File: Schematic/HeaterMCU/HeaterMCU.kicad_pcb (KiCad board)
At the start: 2 copper layers, 100 x 35 mm, 60 parts, among them J301 To PSU Board, J302 Heater Control, J303 High voltage warning, J304 Firmware, SW301 RESET, U301 Display_IPS_1.3_SPI, U302 ATMEGA328P-AU, U303 TLP185, U304 INA219AIDCNR, U305 TLP185, U306 TPS54302, Y301 8MHz

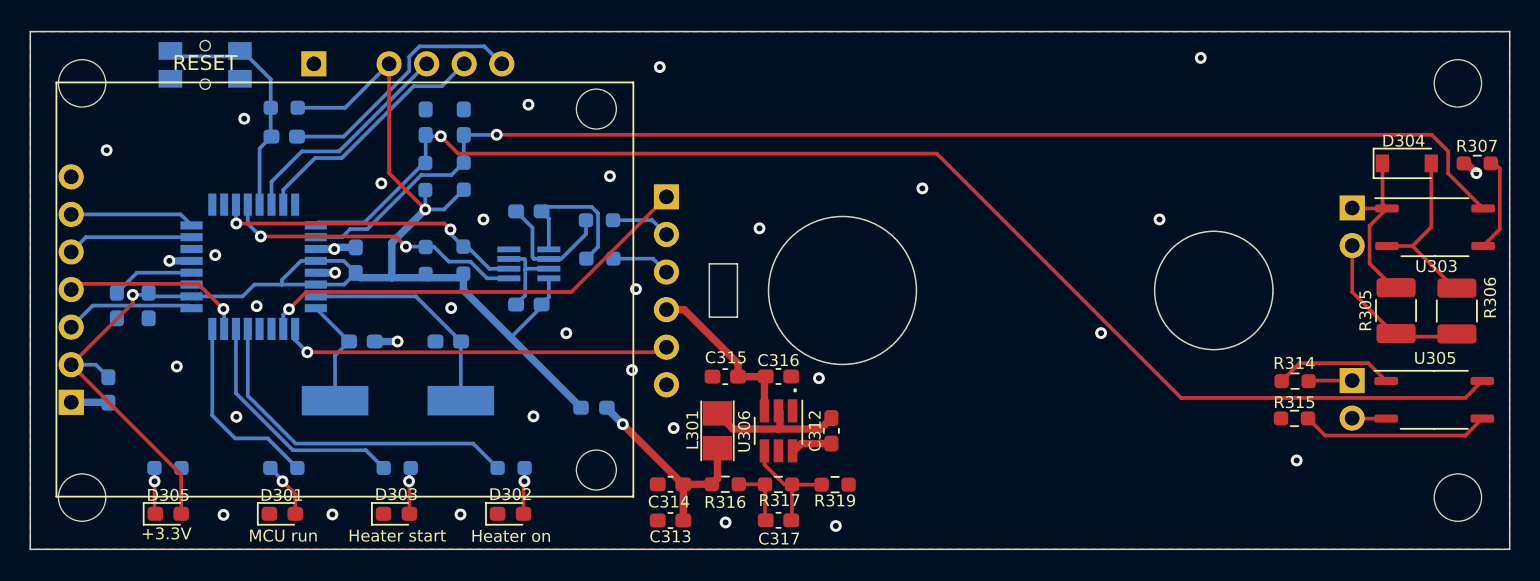
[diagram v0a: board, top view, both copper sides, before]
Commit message: New PSU based on XL4005
Added current limiter
Added interface to uTracer PIC
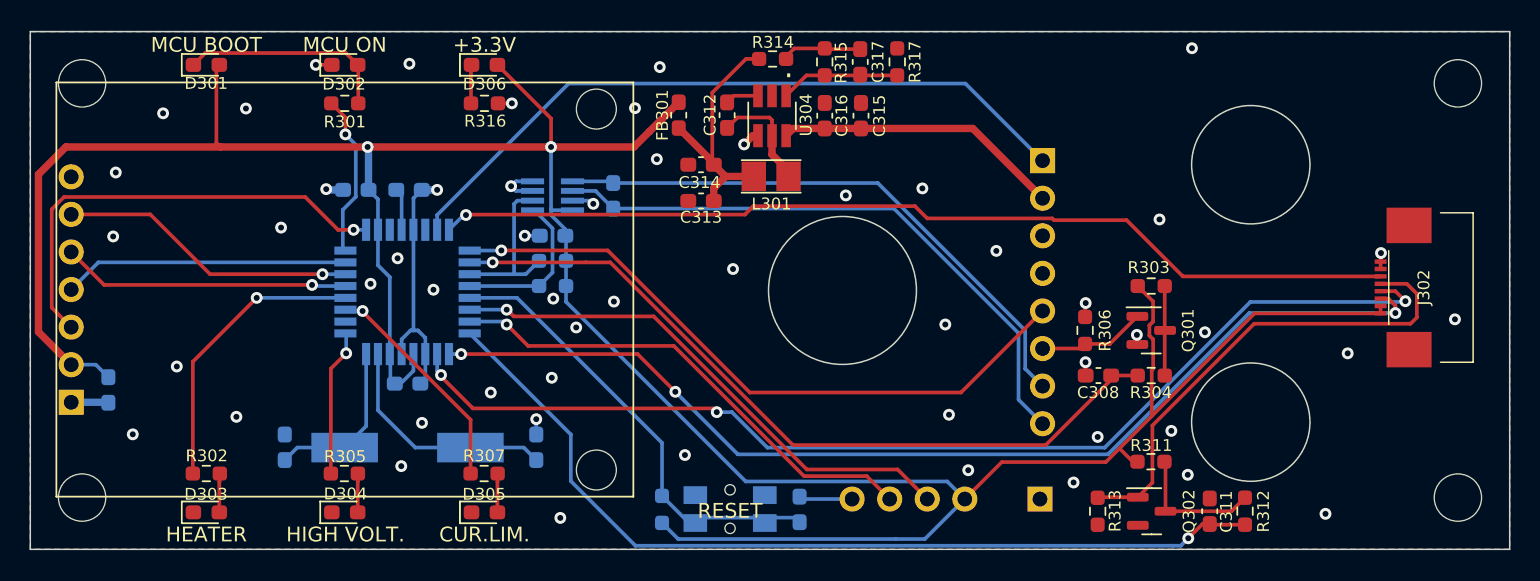
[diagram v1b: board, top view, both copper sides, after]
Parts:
- removed the C303 at (63.0, 63.5)
- removed the D304 at (148.0, 53.9)
- removed the J303 at (144.3, 68.6)
- removed the R305 at (147.3, 63.9)
- removed the R314 at (140.5, 68.6)
- removed the R315 at (140.5, 71.2)
- removed the U303 at (150.0, 58.2)
- removed U305: TLP185, Package_SO:SOIC-4_4.55x3.7mm_P2.54mm
- added C305: 100nF, Capacitor_SMD:C_0603_1608Metric_Pad1.08x0.95mm_HandSolder, B.Cu at (77.0, 55.7)
- added D301: "MCU_BOOT", LED_SMD:LED_0603_1608Metric_Pad1.05x0.95mm_HandSolder, F.Cu at (66.9, 47.2)
- added D305: "Current limit", LED_SMD:LED_0603_1608Metric_Pad1.05x0.95mm_HandSolder, F.Cu at (85.7, 77.5)
- added Q301: BSS138, Package_TO_SOT_SMD:SOT-23, F.Cu at (130.8, 65.2)
- added Q302: BSS138, Package_TO_SOT_SMD:SOT-23, F.Cu at (130.8, 77.4)
- added R303: 1MΩ, Resistor_SMD:R_0603_1608Metric_Pad0.98x0.95mm_HandSolder, F.Cu at (130.8, 62.2)
- C308, C311: value 220nF -> 1µF; moved to F.Cu
- D303: renamed from D302; value "Heater_ON" -> HEATER
- D304: renamed from D303; value "Heater_Start" -> "High Voltage"
- D306: renamed from D305; value "+5V" -> "+3.3V"
- FB301: moved to F.Cu
- J301: footprint Connector_PinSocket_2.54mm:PinSocket_1x06_P2.54mm_Vertical -> Connector_PinHeader_2.54mm:PinHeader_1x08_P2.54mm_Vertical
- J302: value Heater Control -> To µTracer; footprint Connector_PinSocket_2.54mm:PinSocket_1x02_P2.54mm_Horizontal -> myDevices:0527450897; moved to F.Cu
- R301, R302: value 560Ω -> 330Ω; moved to F.Cu
- R304, R312: value 1MΩ -> 220Ω; moved to F.Cu
- R305: renamed from R303; value 560Ω -> 330Ω; moved to F.Cu
- R306: value 3.9kΩ 1/2W -> 100kΩ; footprint Resistor_SMD:R_1210_3225Metric_Pad1.30x2.65mm_HandSolder -> Resistor_SMD:R_0603_1608Metric_Pad0.98x0.95mm_HandSolder
- R307: value 220Ω -> 330Ω
- R311: value 10Ω -> 1MΩ; moved to F.Cu
- R313: value 10Ω -> 100kΩ; moved to F.Cu
- R316: renamed from R318; moved to F.Cu
- moved R307 70.3 mm to (85.7, 74.9), turned to 180 degrees
- moved R312 59.8 mm to (137.1, 77.4)
- moved C311 59.2 mm to (134.7, 77.4)
- moved J303 57.2 mm to (123.2, 76.6), turned to 90 degrees
- moved R304 48.4 mm to (130.8, 68.2), turned to 0 degrees
- moved SW301 46.8 mm to (102.3, 77.5), turned to 180 degrees
- moved C308 46.2 mm to (127.2, 68.2), turned to 0 degrees
- moved C310 43.0 mm to (107.0, 77.3), turned to -90 degrees
- moved R311 39.7 mm to (130.8, 74.1)
- moved R313 39.0 mm to (127.2, 77.4), turned to -90 degrees
- moved R308 37.3 mm to (97.7, 77.3), turned to 90 degrees
- moved D306 37.1 mm to (85.7, 47.2)
- moved R316 32.6 mm to (85.7, 49.9)
- moved C317 31.5 mm to (111.1, 47.0), turned to 90 degrees
- moved D302 30.6 mm to (76.3, 47.2)
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- renumbered C306 to C301, C301 to C302, C309 to C303, C302 to C304, C304 to C306, C305 to C307, C307 to C309, D301 to D302, J304 to J303, R316 to R314, R317 to R315, R319 to R317, U304 to U301, U301 to U302, U302 to U303, U306 to U304
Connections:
- net LED_MCU_ON renamed LED_MCU_STATUS
- C303 pad 1: Net-(C309-Pad1) -> INA_CSENS
- C303 pad 2: Net-(C309-Pad2) (its old number) -> INA_VSENS
- C308 pad 2: FlagMBHeaterActive -> CUR_LIM_FILT
- C311 pad 2: FlagHighVoltage -> FlagHeater
- J301 pad 1: Heater_PWM -> PSU_EN
- J301 pad 2: HeaterSense2 -> VDC
- J301 pad 3: HeaterSense1 -> GNDPWR
- J301 pad 4: VDC -> GNDPWR
- J301 pad 5: Heater_EN -> OUT_EN
- J301 pad 6: GNDPWR -> CUR_LIM
- J302 pad 1: Net-(D304-Pad1) -> +3V3
- J302 pad 2: Net-(J302-Pad2) -> +3V3
- R302 pad 2: LED_Heater_ON -> LED_Heater
- R304 pad 1: +3V3 -> CUR_LIM_FILT
- R304 pad 2: FlagMBHeaterActive -> Net-(Q301-Pad3)
- R305 pad 2: LED_Heater_Start -> LED_HighVoltage
- R306 pad 1: Net-(D304-Pad2) (its old number) -> CUR_LIM
- R306 pad 2: Net-(J302-Pad2) -> GNDPWR
- R307 pad 1: GNDPWR -> Net-(D305-Pad2)
- R307 pad 2: Net-(R307-Pad2) -> LED_CurrentLimit
- R311 pad 1: Net-(C309-Pad2) (its old number) -> +3V3
- R311 pad 2: HeaterSense1 -> Net-(Q302-Pad3)
- R312 pad 1: +3V3 -> FlagHeater
- R312 pad 2: FlagHighVoltage -> Net-(Q302-Pad3)
- R313 pad 1: Net-(C309-Pad1) -> Net-(J302-Pad5)
- R313 pad 2: HeaterSense2 -> GNDPWR
- U301 pad 1: Net-(C309-Pad2) (its old number) -> INA_VSENS
- U301 pad 2: Net-(C309-Pad1) -> INA_CSENS
- U303 pad 1: FlagHighVoltage -> Spare2
- U303 pad 10: Heater_PWM -> unconnected-(U303-Pad10)
- U303 pad 11: unconnected-(U302-Pad11) -> LED_CurrentLimit
- U303 pad 12: unconnected-(U302-Pad12) -> LED_Heater
- U303 pad 13: LED_Heater_ON -> Disp_RES
- U303 pad 14: LED_Heater_Start -> Disp_DC
- U303 pad 2: FlagMBHeaterActive -> Spare1
- U303 pad 23: Disp_RES -> PSU_EN
- U303 pad 24: Disp_DC -> FlagHighVoltage
- U303 pad 25: unconnected-(U302-Pad25) -> OUT_EN
- U303 pad 26: unconnected-(U302-Pad26) -> CUR_LIM_FILT
- U303 pad 32: unconnected-(U302-Pad32) -> FlagHeater
- U303 pad 9: Heater_EN -> LED_HighVoltage
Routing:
- net +3V3: track 97.6 -> 206.0 mm
- net FlagMBHeaterActive: track 85.8 -> 0.00 mm, vias 1 -> 0
- net Spare1: track 0.00 -> 74.9 mm, vias 0 -> 3
- net Spare2: track 0.00 -> 72.4 mm, vias 0 -> 3
- net FlagHeater: track 0.00 -> 60.8 mm, vias 0 -> 1
- net CUR_LIM_FILT: track 0.00 -> 52.4 mm, vias 0 -> 1
- net PSU_EN: track 0.00 -> 47.8 mm
- net OUT_EN: track 0.00 -> 45.0 mm, vias 0 -> 1
- net INA_CSENS: track 0.00 -> 40.9 mm
- net INA_VSENS: track 0.00 -> 39.0 mm
- net Net-(J302-Pad5): track 0.00 -> 33.2 mm
- net Heater_PWM: track 30.2 -> 0.00 mm, vias 1 -> 0
- net Heater_EN: track 26.3 -> 0.00 mm, vias 1 -> 0
- net FlagHighVoltage: track 90.4 -> 65.6 mm
- net LED_Heater_ON: track 23.4 -> 0.00 mm
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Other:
- outline, holes or cut-outs redrawn
- board text added: "CUR.LIM."
- board text added: "HEATER"
- board text added: "HIGH VOLT."
- board text added: "MCU BOOT"
- board text added: "MCU ON"
- board text added: "µTracer Heater MCU 22_43_0120D Bjørner Sandom"
- board text removed: "GND"
- board text removed: "Heater on"
- board text removed: "Heater start"
- board text removed: "K A From MB HV LED"
- board text removed: "MCU run"
- board text removed: "R L From MB heater"
- board text removed: "µTracer Heater MCU 22_43_0120C Bjørner Sandom"

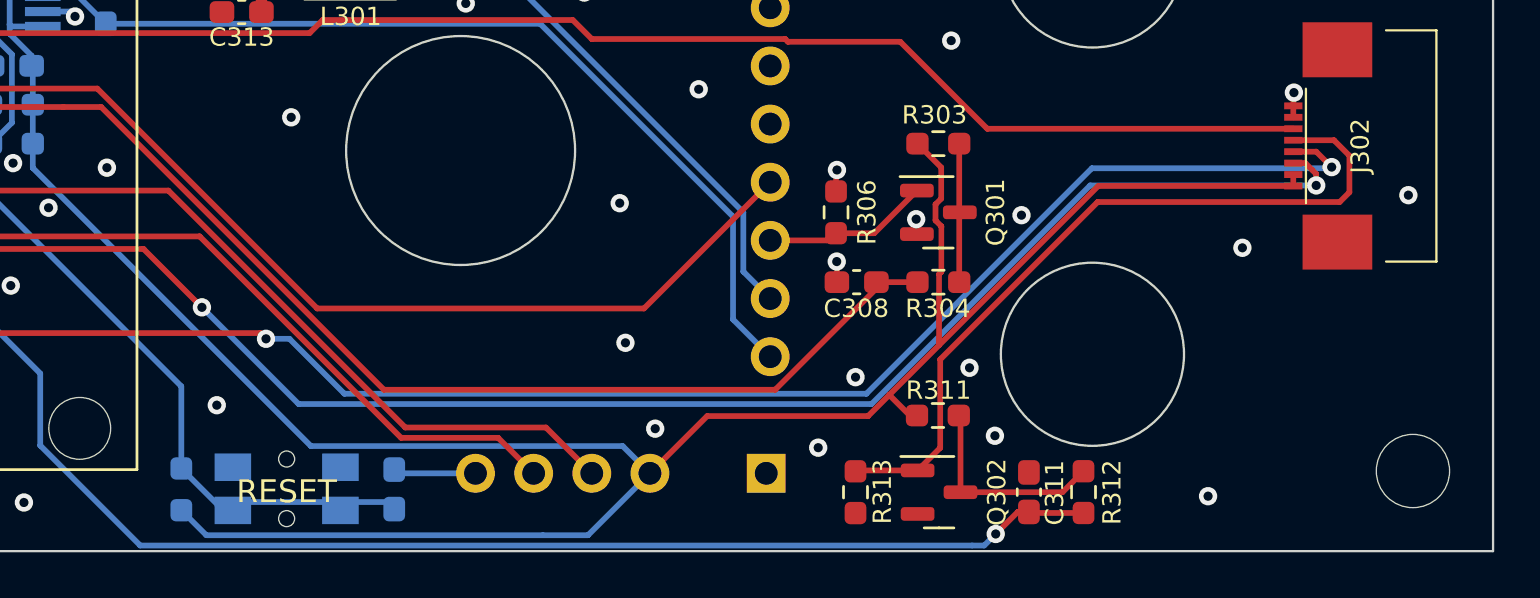
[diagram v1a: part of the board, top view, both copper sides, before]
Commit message: PIC interface board, version A
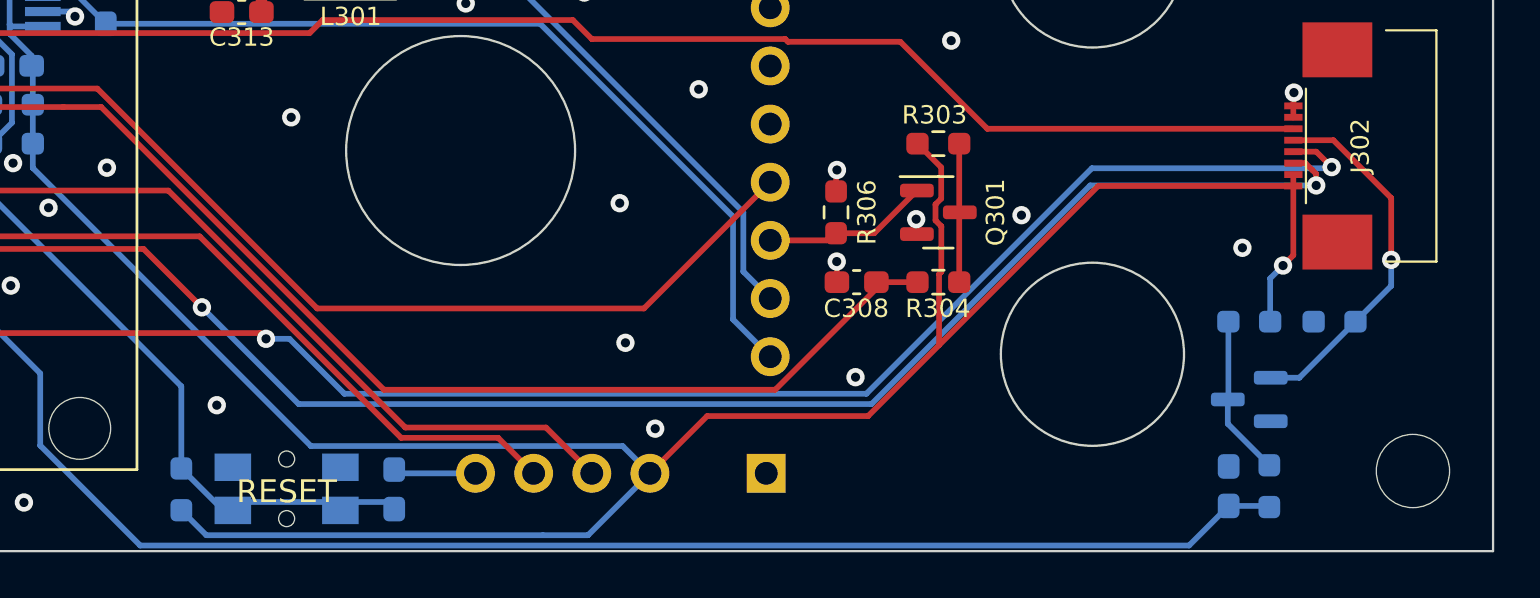
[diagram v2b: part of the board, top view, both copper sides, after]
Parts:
- C311, Q302, R311, R312, R313: moved to B.Cu
- moved R313 22.2 mm to (148.1, 70.0), turned to 180 degrees
- moved R311 14.2 mm to (144.3, 70.0), turned to 180 degrees
- moved Q302 14.1 mm to (144.3, 73.4), turned to 180 degrees
- moved C311 8.73 mm to (143.4, 77.2)
- moved R312 8.12 mm to (145.2, 77.2)
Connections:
- net FlagHeater renamed FlagHeater_FILT
- net Net-(J302-Pad5) renamed /FlagHeater
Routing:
- net /FlagHeater: track 33.2 -> 16.1 mm, vias 0 -> 1
- net FlagHeater_FILT: track 60.8 -> 69.1 mm, vias 1 -> 0
- net +3V3: track 206.0 -> 210.8 mm, vias 2 -> 3
- net Net-(Q302-Pad3): track 9.13 -> 7.04 mm
- net GNDPWR: vias 54 -> 49

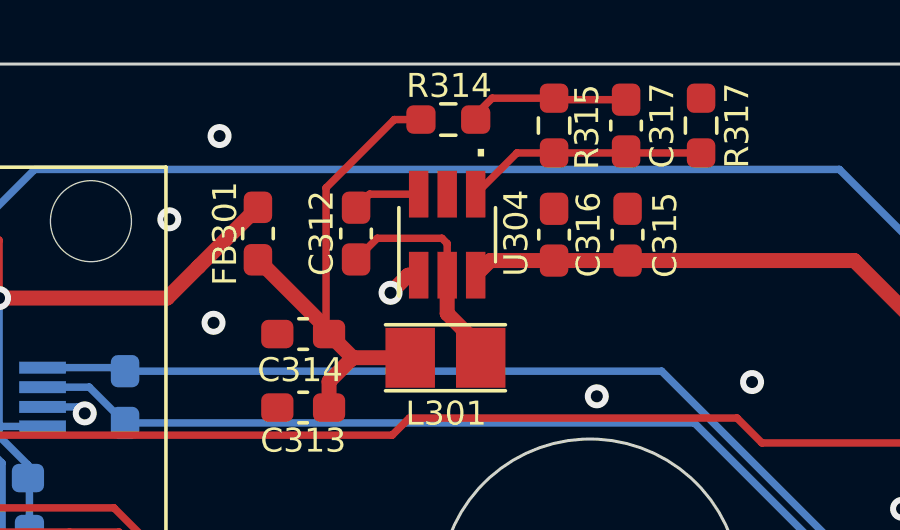
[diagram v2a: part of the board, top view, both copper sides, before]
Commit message: Updated component values
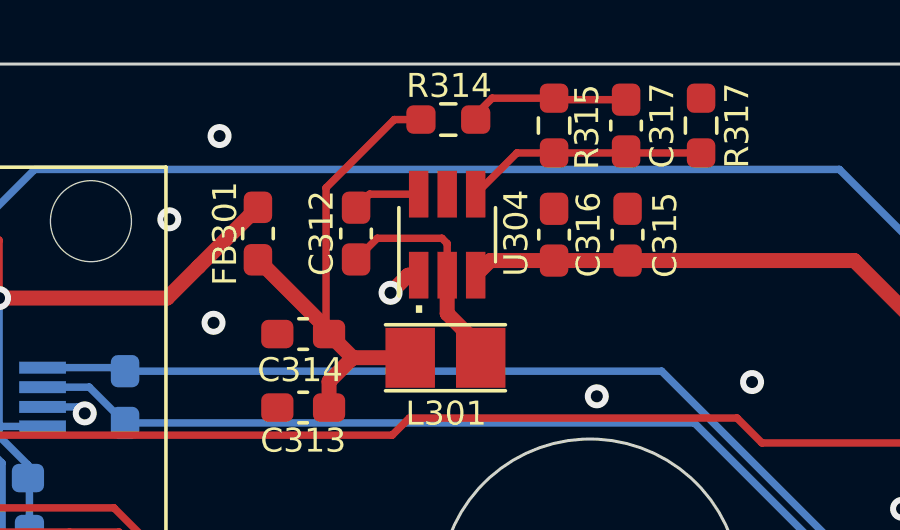
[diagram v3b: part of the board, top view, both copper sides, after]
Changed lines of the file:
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@@
     (effects (font (size 1 1) (thickness 0.15)) (justify mirror))
+  )
+  (gr_text "." (at 83.3 67.2) (layer "B.SilkS")
+    (effects (font (size 1.5 1.5) (thickness 0.3)) (justify mirror))
+  )
+  (gr_text "." (at 92.9 54.5) (layer "B.SilkS")
+    (effects (font (size 1.5 1.5) (thickness 0.3)) (justify mirror))
   )
   (gr_text "RESET" (at 102.2 74.8) (layer "B.SilkS")
@@
     (effects (font (size 1 1) (thickness 0.15)))
   )
-  (gr_text "." (at 106.2625 47.3875) (layer "F.SilkS")
+  (gr_text "." (at 104.2 52.6) (layer "F.SilkS")
     (effects (font (size 1.5 1.5) (thickness 0.3)))
   )

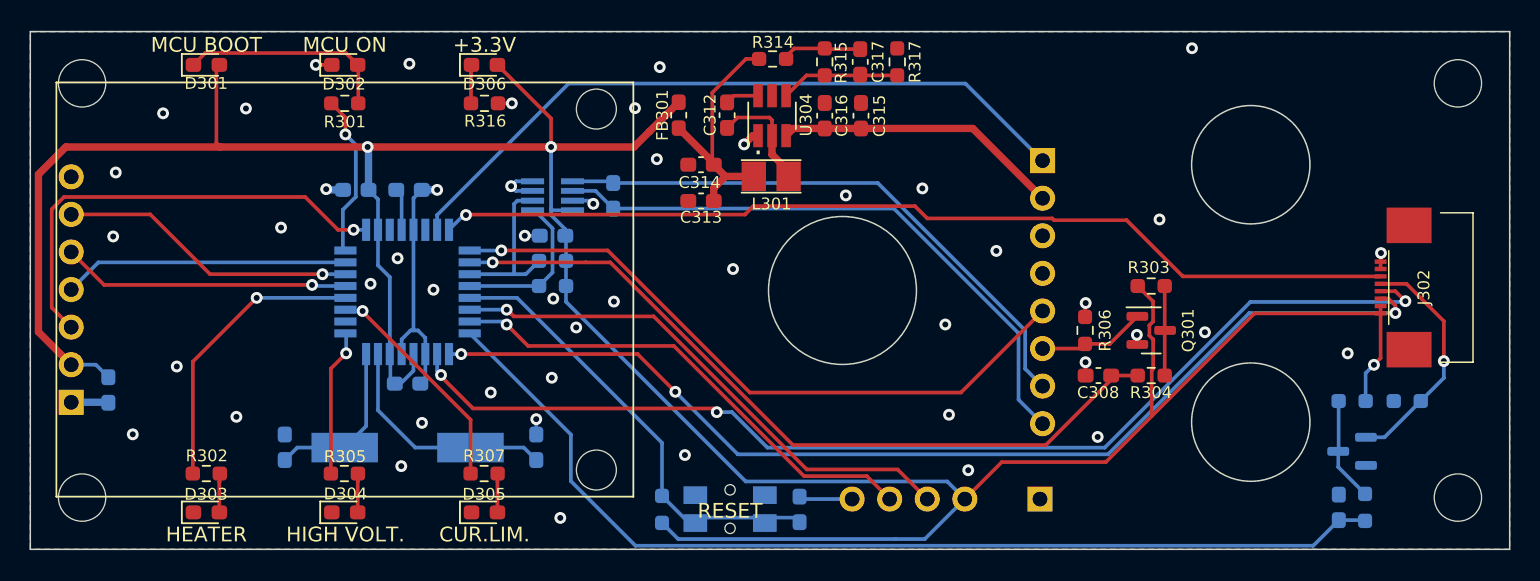
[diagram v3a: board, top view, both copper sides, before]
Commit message: Changed pin for MCU status LED
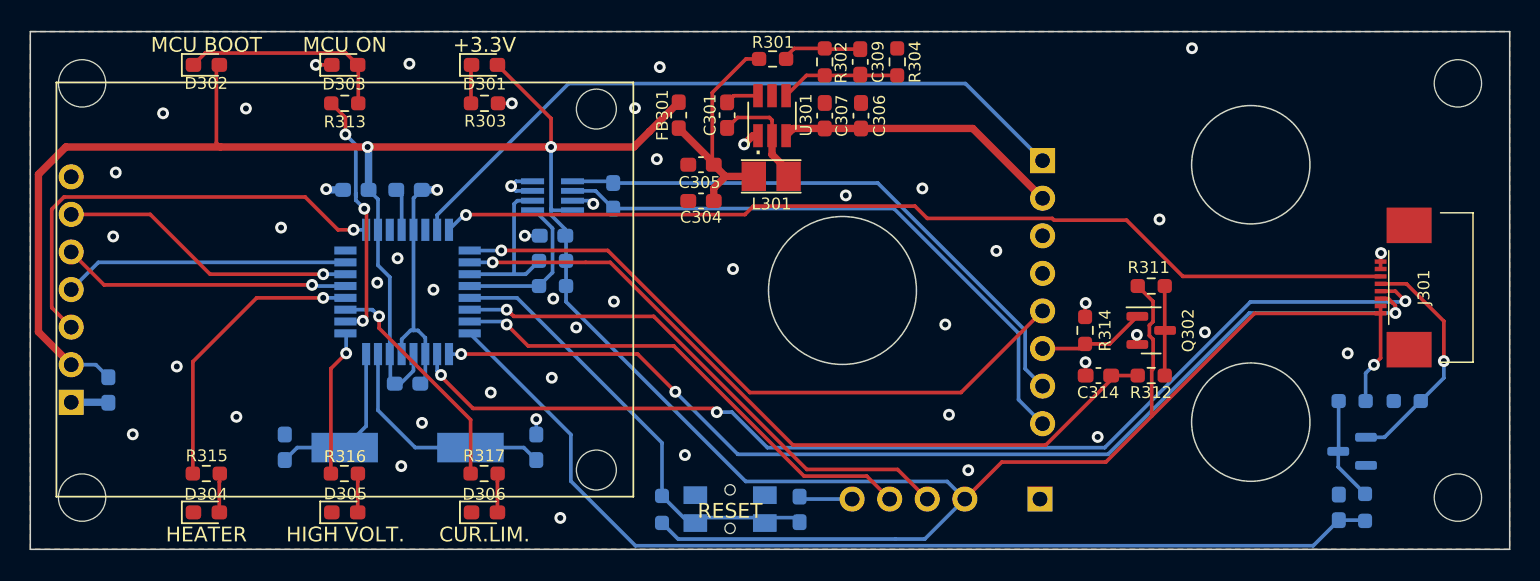
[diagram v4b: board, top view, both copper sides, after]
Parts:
- R303: renamed from R316; value 330Ω -> 560Ω
- R313: renamed from R301; value 330Ω -> 560Ω
- R315: renamed from R302; value 330Ω -> 560Ω
- renumbered C312 to C301, C304 to C302, C305 to C303, C313 to C304, C314 to C305, C315 to C306, C316 to C307, C306 to C308, C317 to C309, C307 to C310, C309 to C311, C311 to C312, C310 to C313, C308 to C314, C301 to C315, C302 to C316, C303 to C317, D306 to D301, D301 to D302, D302 to D303, D303 to D304, D304 to D305, D305 to D306, J302 to J301, J303 to J302, J301 to J303, Q302 to Q301, Q301 to Q302, R314 to R301, R315 to R302, R317 to R304, R311 to R305, R312 to R306, R308 to R307, R309 to R308, R310 to R309, R313 to R310, R303 to R311, R304 to R312, R306 to R314, R305 to R316, R307 to R317, U304 to U301, U303 to U302, U301 to U303, U302 to U304
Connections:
- net CUR_LIM_FILT renamed FLAG_CUR_LIM_FILT
- net Disp_DC renamed DISP_DC
- net Disp_RES renamed DISP_RST
- net Disp_SCL renamed DISP_SCL
- net Disp_SDA renamed DISP_SDA
- net FlagHeater_FILT renamed FLAG_HEATER_FILT
- net FlagHighVoltage renamed FLAG_HIGH_VOLTAGE
- net LED_CurrentLimit renamed LED_CURRENT_LIMIT
- net LED_Heater renamed LED_HEATER
- net LED_HighVoltage renamed LED_HIGH_VOLTAGE
- U302 pad 10: unconnected-(U303-Pad10) -> LED_MCU_STATUS
- U302 pad 16: LED_MCU_STATUS -> unconnected-(U302-Pad16)
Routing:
- net LED_MCU_STATUS: track 11.1 -> 17.2 mm, vias 1 -> 3
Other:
- board text added: "µTracer Heater MCU 22_43_0120E Bjørner Sandom"
- board text removed: "µTracer Heater MCU 22_43_0120D Bjørner Sandom"
